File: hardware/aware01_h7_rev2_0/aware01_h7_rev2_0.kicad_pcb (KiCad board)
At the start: 4 copper layers, 46 x 110 mm, 156 parts, among them IC1 587-2054-127F, IC2 587-2054-127F, IC3 587-2054-127F, IC4 587-2054-127F, IC5 TLV320AIC3204IRHBR, J1 Conn_02x07_Odd_Even, J10 GATE4_IN, J11 CV2_IN, J12 CV3_IN, J13 V/OCT_IN, J14 CV1_IN, J2 Conn_02x05_Odd_Even, J3 InL, J4 InR, J5 OutL, J6 OutR, J7 GATE1_IN, J8 GATE2_IN, J9 GATE3_IN, Q1 MMBT3904, Q2 MMBT3904, Q3 MMBT3904, Q4 MMBT3904, SW1 SW_Push, SW2 SW_Push, U1 LMR50410Y5FQDBVRQ1, U10 NE5532DRG4, U11 NE5532DRG4, U12 OPA2322AIDR, U13 OPA2322AIDR, U2 LM1117MP-3.3, U3 74AHCT1G14DBVRG4, U4 STM32H7A3RITx, U5 LM4040DIM3X-10, U6 10k, U7 10k, U8 10k, U9 10k, Y1 WE-XTAL 24.0MHz 50ppm

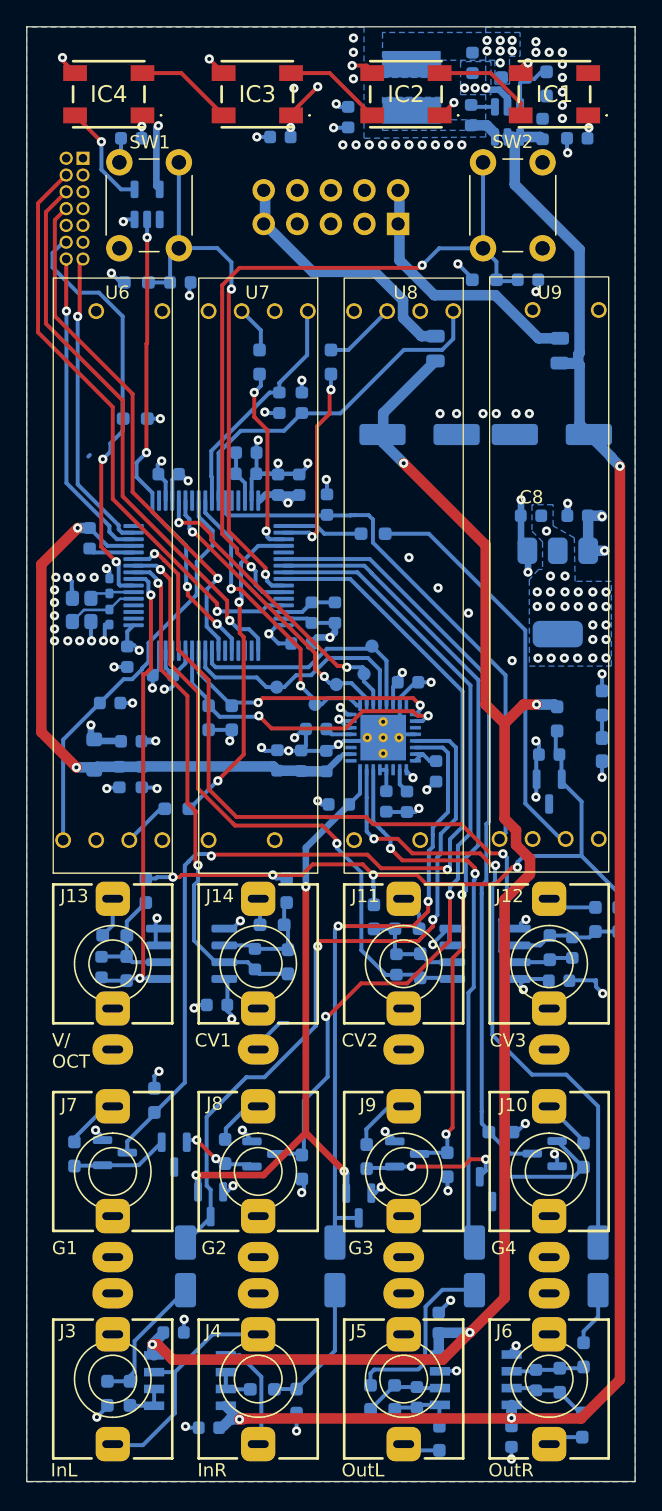
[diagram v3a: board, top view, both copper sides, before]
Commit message: hw: Improve routing and layouting
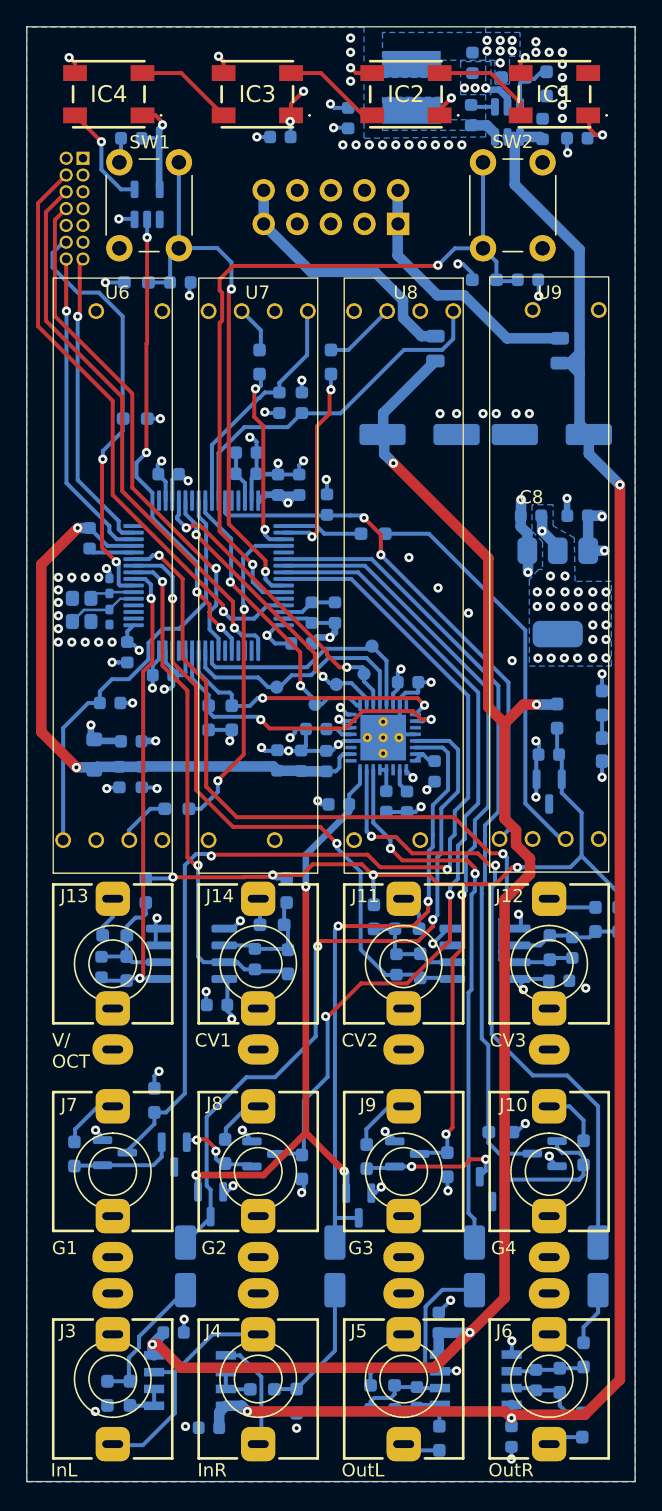
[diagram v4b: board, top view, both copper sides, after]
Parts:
- removed G***: LOGO, LOGO
- moved C3 0.34 mm to (137.8, 89.7)
- moved R7 0.21 mm to (170.3, 94.5)
- moved R27 0.18 mm to (172.3, 127.5)
- moved C39 0.11 mm to (161.0, 98.7)
- moved C30 0.08 mm to (154.5, 49.3)
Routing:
- net GND: track 132.1 -> 117.3 mm, vias 111 -> 109
- net +3.3V: track 45.3 -> 49.3 mm
- net +5V: track 20.6 -> 23.4 mm, vias 16 -> 15
- net Net-(Q4-B): track 9.07 -> 10.4 mm
- net /FADER1_IN: track 31.2 -> 32.4 mm
- net /GATE4_IN: track 57.9 -> 59.1 mm
- net /CV1_IN: track 39.0 -> 40.1 mm
- net /I2C1_SCL: track 20.8 -> 21.7 mm
- net Net-(J10-PadT): track 3.99 -> 4.90 mm
- net /GATE1_IN: track 75.3 -> 76.2 mm
- net /CV3_IN: track 59.4 -> 60.1 mm
- net Net-(U11A--): track 6.07 -> 6.81 mm
- net /I2C1_SDA: track 23.9 -> 24.6 mm
- net /BUTTON2_IN: track 58.2 -> 58.9 mm
- net /Audio Codec/Input Output Channels/OUTL: track 42.2 -> 42.9 mm
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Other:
- board text added: "Jonas Lux 2026 01"

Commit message: hw: improve layout, update BOM
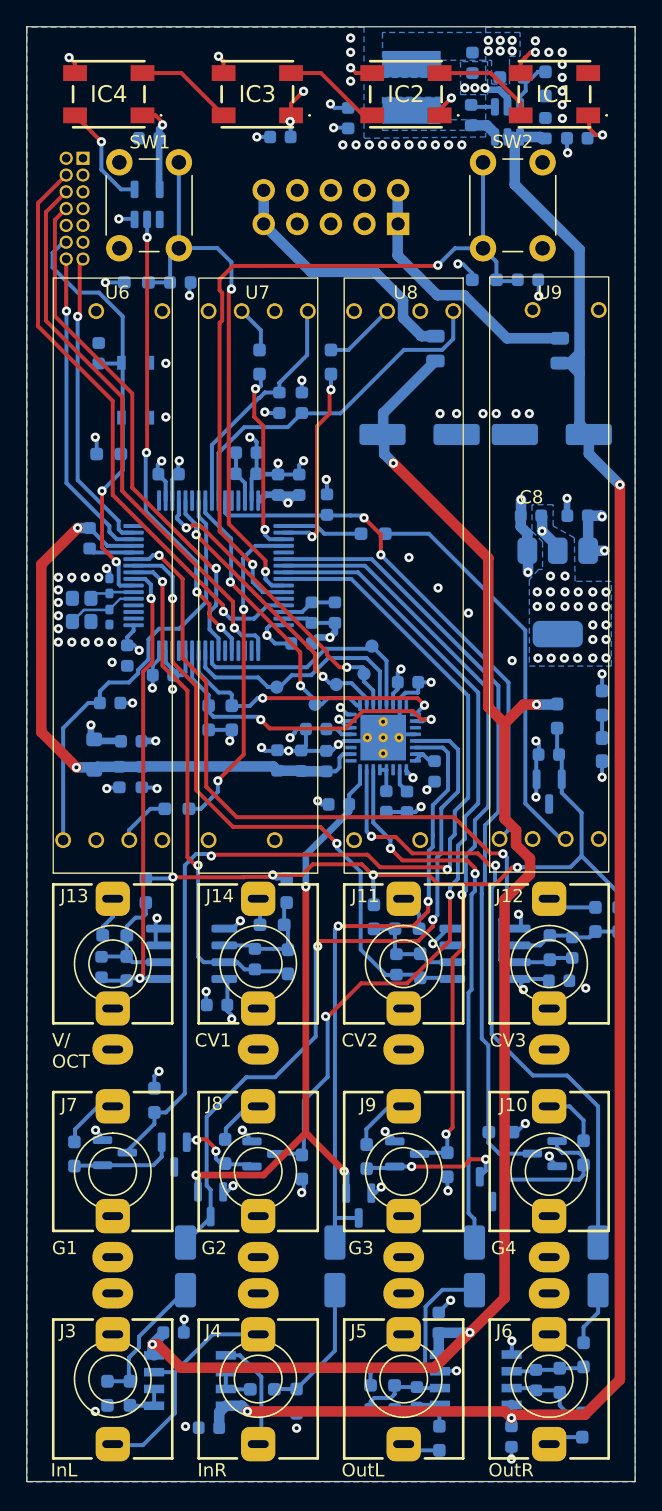
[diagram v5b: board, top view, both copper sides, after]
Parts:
- added C5: 100n, Capacitor_SMD:C_0603_1608Metric, B.Cu at (135.6, 67.1)
- added SW3: PTS815, Button_Switch_SMD:SW_SPST_PTS810, B.Cu at (138.4, 69.8)
- moved R4 3.34 mm to (136.4, 74.7), turned to 0 degrees
- moved C34 1.35 mm to (139.4, 50.8)
- moved C3 0.25 mm to (137.8, 89.9)
- moved C2 0.23 mm to (169.4, 50.0)
- moved R2 0.13 mm to (166.9, 46.2)
- moved R3 0.08 mm to (169.4, 46.7)
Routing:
- net GND: track 117.3 -> 114.3 mm, vias 109 -> 110
- net /NRST: track 31.9 -> 33.6 mm
- net +5V: track 23.4 -> 22.3 mm, vias 15 -> 14
- net +3.3V: track 49.3 -> 50.0 mm
- net /RGB_LED_DATA: track 35.9 -> 35.4 mm
- net Net-(U1-FB): track 3.84 -> 4.39 mm
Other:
- board text added: "RST"

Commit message: hw: improve layout
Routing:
- net /BUTTON2_IN: track 58.9 -> 57.2 mm
- net -12V: track 117.8 -> 118.5 mm

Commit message: hw: update BOM and layout
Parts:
- added C9: 10u, Capacitor_SMD:C_0603_1608Metric, B.Cu at (171.2, 50.0)
- moved C27 1.37 mm to (173.0, 50.1), turned to 90 degrees
- moved C3 0.39 mm to (137.4, 89.9)
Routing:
- net +12V: track 138.2 -> 140.0 mm
- net GND: track 114.3 -> 112.8 mm, vias 110 -> 108
- net +3.3V: track 50.0 -> 51.4 mm
- net Net-(U9B-A): track 30.9 -> 29.8 mm
- net /Audio Codec/Input Output Channels/OUTR: track 48.8 -> 49.4 mm
- net /Audio Codec/Input Output Channels/OUTL: track 42.9 -> 42.2 mm
- net Net-(IC5-IN2_L): track 2.55 -> 1.96 mm
